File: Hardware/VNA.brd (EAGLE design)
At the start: 122 x 98 mm, 503 parts, among them IC1 MIC2253, IC10 MAX2871, IC11 RFSW6042, IC12 RFSW6042, IC13 QPC6324, IC14 RFSA3714, IC15 TRF37A73, IC16 QPC6324, IC17 QPC6324, IC18 QPC6324, IC19 AP2114H, IC2 LM3370SD-4221, IC20 NCP702-3.3, IC21 MAX2871, IC22 LT5560, IC23 THS4521IDGKR, IC24 ADL5801, IC25 NCP702-1.8, IC26 MCP33131D-10-E/MS, IC27 LT5560, IC28 THS4521IDGKR, IC29 ADL5801, IC3 LDL212PU50R, IC30 NCP702-1.8, IC31 MCP33131D-10-E/MS, IC32 THS4521IDGKR, IC33 ADL5801, IC34 NCP702-1.8, IC35 MCP33131D-10-E/MS, IC36 LT5560, IC37 STM32G431CB, IC4 LDL212PU50R, IC5 LDL212PU50R, IC6 LDL212PU50R, IC7 SI5351C, IC8 AP2114H, IC9 NCP702-3.3, J1 PJ-014D, J2 AMPHENOL_132289, J3 AMPHENOL_132289, J4 TYPE-C16P(073), Q1 SSM3J338R, Q2 SSM3J338R, T1 B012-617DB-1-63-B331, T2 B012-617DB-1-63-B331, T3 B012-617DB-1-63-B331, U1 W25Q16BVSN, U2 6SLX9TQG144, X1 SMA_CONNECTOR, X2 SMA_CONNECTOR, Y1 DSB221SDN/26MHz

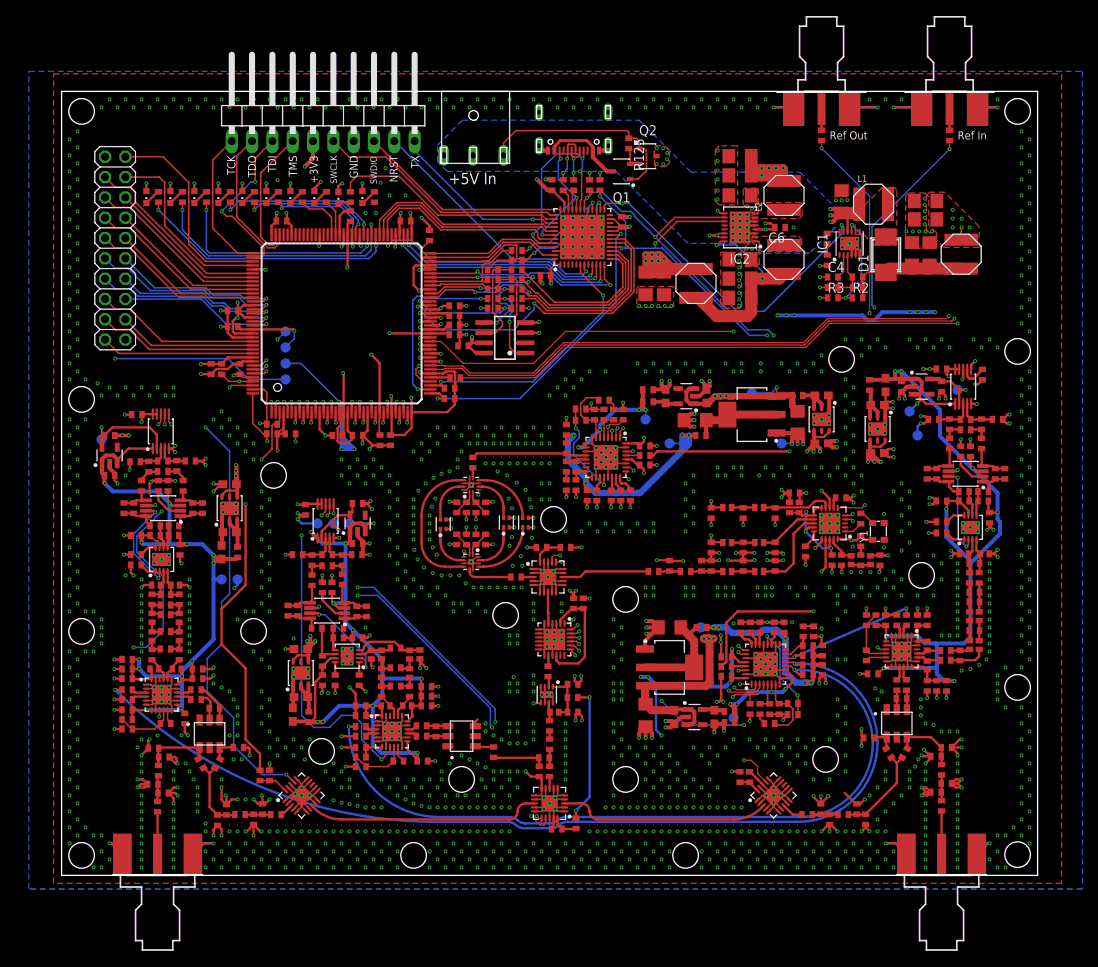
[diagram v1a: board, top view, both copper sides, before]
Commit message: Additional filters for digital control lines, attenuator for Port1/Ref 1.LO
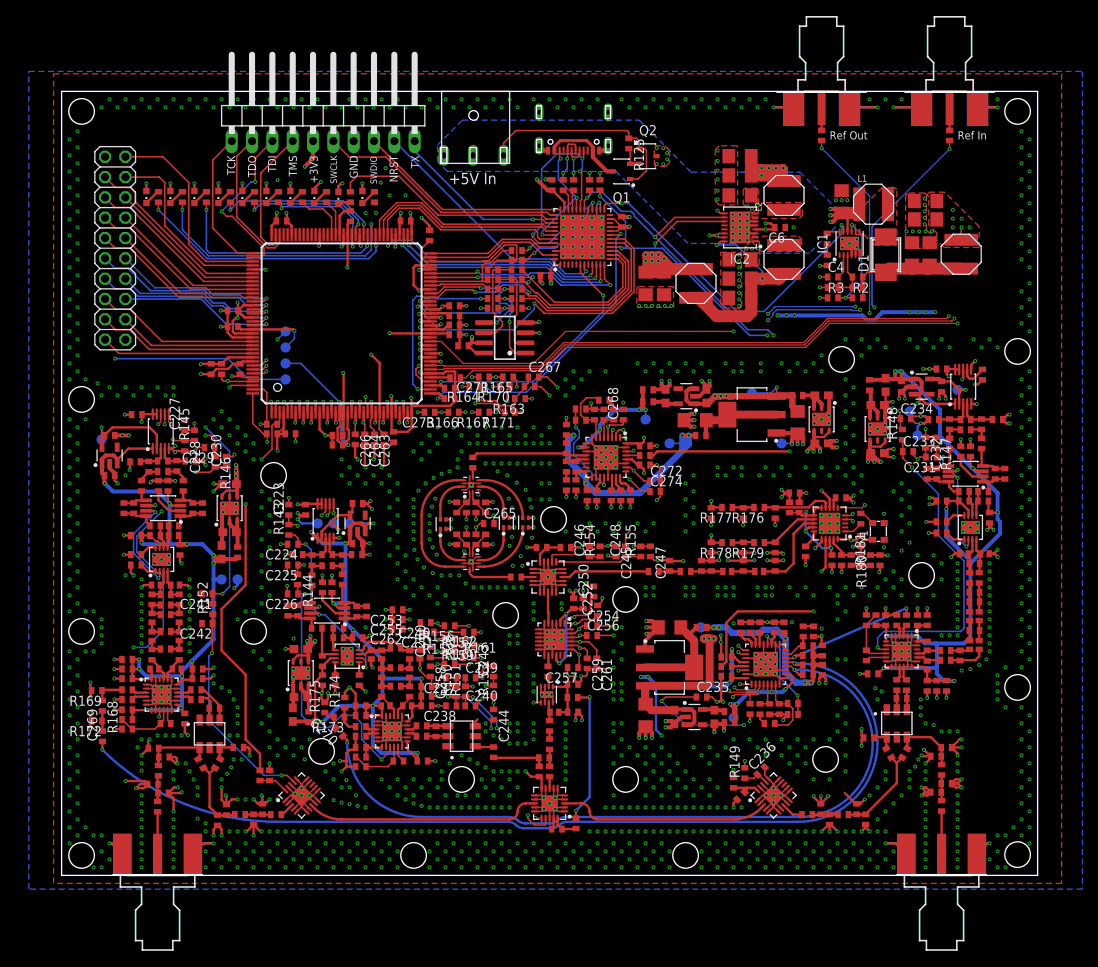
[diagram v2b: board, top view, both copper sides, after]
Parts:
- removed L11, L12, L13, L15, L16, L17: 120n, VNA:L0402
- added C223, C224, C225, C226, C227, C228, C229, C230, C231, C232, C233, C234, C235, C236, C237, C238, C239, C240, C241, C242, C243, C244, C245, C246, C247, C248, C249, C250, C251, C252, C253, C254, C255, C256, C257, C258, C259, C260, C261, C262, C263, C264, C265, C266, C267, C268, C271, C272, C273, C274: 100p, VNA:C0402
- added C269, C270: 100n, VNA:C0402
- added R143, R144, R145, R146, R147, R148, R149, R150, R151, R152, R153, R154, R155, R156, R157, R158, R159, R160, R161, R162, R163, R165, R166: 10k, VNA:R0402
- added R164, R167, R169, R170, R171, R172, R174, R175: 100, VNA:R0402
- added R168, R173: 75, VNA:R0402
- added R176, R177, R178, R179, R180, R181: 0, VNA:R0402
- C35, C36, C37, C44, C45, C46: value 18p -> DNP
- C40, C41, C42: value 56p -> DNP
- moved R11 12.2 mm to (58.5, 59.1), turned to 180 degrees
- moved C210 2.77 mm to (34.5, 51.8), turned to 180 degrees
- moved C77 2.60 mm to (84.9, 7.94), turned to 225 degrees
- moved L26 1.06 mm to (84.0, 9.60)
- moved C212 0.57 mm to (41.5, 52.8)
- moved C213 0.51 mm to (40.3, 52.5)
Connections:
- new net N$169: C225.1, R132.1, R144.1, U2.P144
- new net N$170: C227.1, R131.2, R145.2, U2.P140
- new net N$172: C232.1, R122.2, R147.1, U2.P57
- new net N$173: C229.1, R130.1, R146.1, U2.P141
- new net N$174: C236.1, IC17.17, R149.1
- new net N$176: C240.1, IC16.16, R151.1
- new net N$178: C238.1, IC16.17, R150.1
- new net N$180: C268.1, IC10.4, R163.1
- new net N$182: C242.1, IC18.17, R152.1
- new net N$184: C244.1, IC15.5, R153.1
- new net N$185: C246.1, IC13.17, R154.1
- new net N$192: C250.1, IC14.1, R156.1
- new net N$193: C248.1, IC13.16, R155.1
- new net N$226: IC10.1, R164.1
- new net N$227: C252.1, IC14.24, R157.1
- new net N$232: IC10.2, R170.1
- new net N$257: C254.1, IC14.23, R158.1
- new net N$258: IC10.3, R171.1
- new net N$259: C256.1, IC14.22, R159.1
- new net N$260: C257.1, IC14.19, R160.2
- new net N$261: IC10.30, R167.1
- new net N$262: C259.1, IC14.20, R161.2
- new net N$263: C272.1, IC10.26, R165.1
- new net N$264: C261.1, IC14.21, R162.2
- new net N$265: C269.2, R168.2, R172.1
- new net N$266: C274.1, IC10.25, R166.1
- new net N$267: C114.1, R168.1, R169.1
- new net N$268: C270.2, R173.2, R175.1
- new net N$269: C183.1, R173.1, R174.1
- new net N$312: C223.1, R133.2, R143.2, U2.P143
- new net N$512: C234.1, R121.1, R148.2, U2.P58
- net AMP_PWDN: now also C243.1, R153.2; no longer IC15.5
- net ATT_D0: now also C249.1, R156.2; no longer IC14.1
- net ATT_D1: now also C251.1, R157.2; no longer IC14.24
- net ATT_D2: now also C253.1, R158.2; no longer IC14.23
- net ATT_D3: now also C255.1, R159.2; no longer IC14.22
- net ATT_D4: now also C262.1, R162.1; no longer IC14.21
- net ATT_D5: now also C260.1, R161.1; no longer IC14.20
- net ATT_D6: now also C258.1, R160.1; no longer IC14.19
- net FILT_IN_C1: now also C263.1
- net FILT_IN_C2: now also C264.1
- net FILT_OUT_C1: now also C266.1
- net FILT_OUT_C2: now also C265.1
- net GND: now also C223.2, C224.2, C225.2, C226.2, C227.2, C228.2, C229.2, C230.2, C231.2, C232.2, C233.2, C234.2, C235.2, C236.2, C237.2, C238.2, C239.2, C240.2, C241.2, C242.2, C243.2, C244.2, C245.2, C246.2, C247.2, C248.2, C249.2, C250.2, C251.2, C252.2, C253.2, C254.2, C255.2, C256.2, C257.2, C258.2, C259.2, C260.2, C261.2, C262.2, C263.2, C264.2, C265.2, C266.2, C267.2, C268.2, C271.2, C272.2, C273.2, C274.2, R169.2, R172.2, R174.2, R175.2
- net HIGHBAND_SELECT: now also C245.1, R154.2; no longer IC13.17
- net LOWBAND_SELECT: now also C247.1, R155.2; no longer IC13.16
- net N$101: now also R180.1; no longer L11.1
- net N$160: now also R176.1; no longer L13.1
- net N$91: now also R180.2, R181.1; no longer L11.2, L15.1
- net N$96: now also R178.1, R179.2; no longer L12.2, L16.1
- net N$97: now also R179.1; no longer L12.1
- net N$99: now also R176.2, R177.1; no longer L13.2, L17.1
- net PORT1LO1: now also C269.1; no longer C114.1
- net PORT1LO2: now also R177.2; no longer L17.2
- net PORT1MIX1_EN: now also C230.1, R146.2; no longer R130.1, U2.P141
- net PORT1MIX2_EN: now also C228.1, R145.1; no longer R131.2, U2.P140
- net PORT1SWITCH: now also C241.1, R152.2; no longer IC18.17
- net PORT2LO2: now also R181.2; no longer L15.2
- net PORT2MIX1_EN: now also C233.1, R148.1; no longer R121.1, U2.P58
- net PORT2MIX2_EN: now also C231.1, R147.2; no longer R122.2, U2.P57
- net PORT2SWITCH: now also C235.1, R149.2; no longer IC17.17
- net PORTSWITCH1: now also C239.1, R151.2; no longer IC16.16
- net PORTSWITCH2: now also C237.1, R150.2; no longer IC16.17
- net REFLO1: now also C270.1; no longer C183.1
- net REFLO2: now also R178.2; no longer L16.2
- net REFMIX1_EN: now also C226.1, R144.2; no longer R132.1, U2.P144
- net REFMIX2_EN: now also C224.1, R143.1; no longer R133.2, U2.P143
- net SOURCE_CE: now also C267.1, R163.2; no longer IC10.4
- net SOURCE_CLK: now also R164.2; no longer IC10.1
- net SOURCE_LD: now also C273.1, R166.2; no longer IC10.25
- net SOURCE_LE: now also R171.2; no longer IC10.3
- net SOURCE_MOSI: now also R170.2; no longer IC10.2
- net SOURCE_MUX: now also R167.2; no longer IC10.30
- net SOURCE_RF_EN: now also C271.1, R165.2; no longer IC10.26
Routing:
- net PORT2MIX2_EN: track 109.2 -> 16.7 mm
- net GND: track 714.6 -> 801.6 mm, vias 1683 -> 1701
- net N$172: track 0.00 -> 83.5 mm, vias 0 -> 4
- net N$512: track 0.00 -> 74.5 mm, vias 0 -> 4
- net PORT2MIX1_EN: track 91.7 -> 40.4 mm
- net N$266: track 0.00 -> 29.6 mm, vias 0 -> 2
- net N$169: track 0.00 -> 28.5 mm, vias 0 -> 2
- net PORT1SWITCH: track 62.2 -> 34.2 mm
- net SOURCE_LD: track 35.5 -> 7.86 mm
- net REFMIX1_EN: track 61.7 -> 34.1 mm, vias 3 -> 2
- net N$182: track 0.00 -> 27.3 mm, vias 0 -> 2
- net N$263: track 0.00 -> 27.2 mm, vias 0 -> 2
- net N$178: track 0.00 -> 26.8 mm, vias 0 -> 3
- net N$312: track 0.00 -> 24.6 mm, vias 0 -> 2
- net PORTSWITCH2: track 69.2 -> 44.9 mm, vias 4 -> 2
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
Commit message: 0402 pads reduced in size
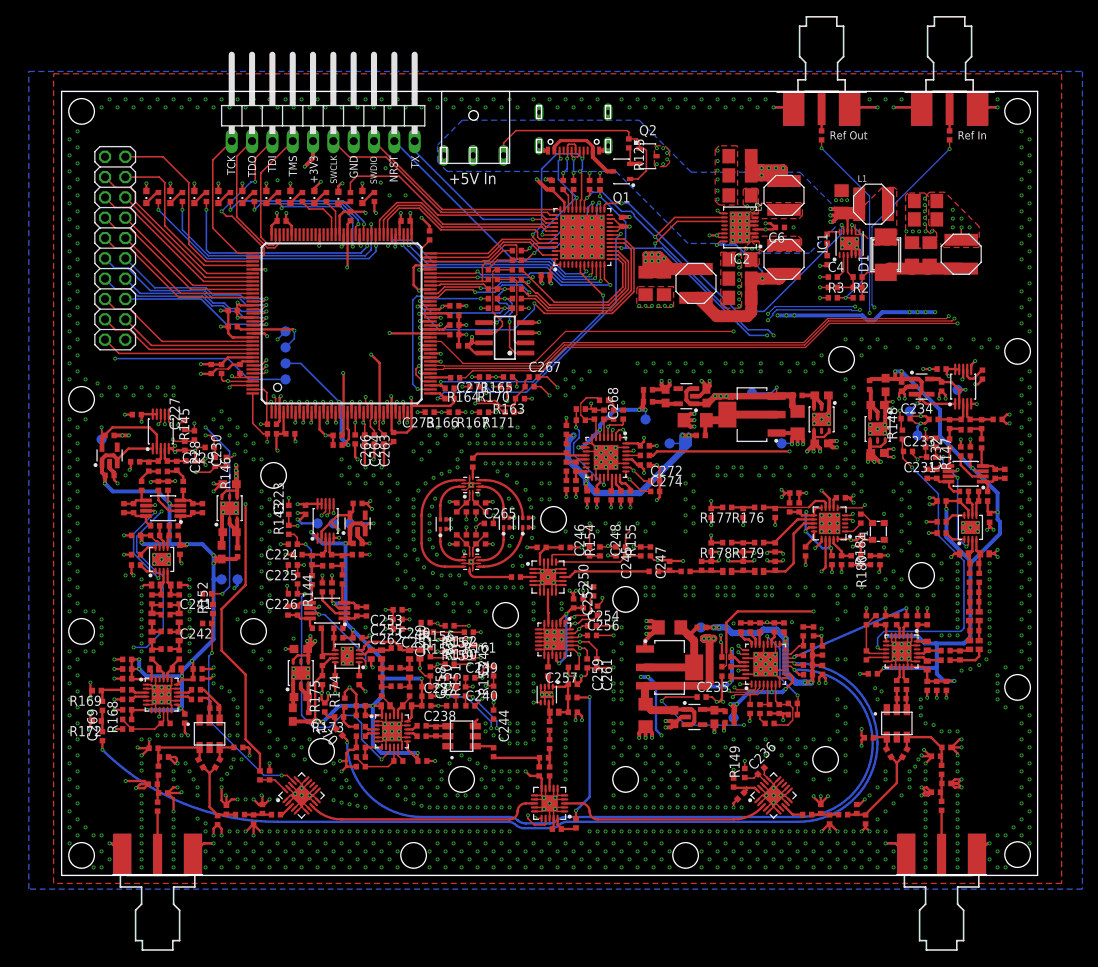
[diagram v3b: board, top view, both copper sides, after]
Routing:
- net GND: track 801.6 -> 814.5 mm, vias 1701 -> 1703
- net +3V3: track 391.4 -> 379.8 mm, vias 68 -> 69
- net N$138: track 38.6 -> 36.6 mm
- net REF_SDO: track 19.8 -> 21.4 mm
- net N$128: track 11.0 -> 12.2 mm
- net +5V/2: track 119.7 -> 120.8 mm
- net N$58: track 4.17 -> 5.22 mm
- net +5V/1: track 100.9 -> 101.9 mm
- net HIGHBAND_SELECT: track 47.2 -> 46.3 mm
- net OUT+2: track 2.47 -> 3.11 mm
- net SOURCE_VCC: track 85.3 -> 84.8 mm
- net N$110: track 36.8 -> 37.3 mm

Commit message: Silkscreen adjustments
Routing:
- net +3V3: track 379.8 -> 386.6 mm
- net GND: vias 1703 -> 1691
